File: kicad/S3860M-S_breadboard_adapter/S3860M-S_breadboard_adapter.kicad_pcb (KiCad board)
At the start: 2 copper layers, 26.9 x 36.3 mm, 4 parts, among them P1 CONN_01X12, P2 CONN_01X12, U1 XS3860

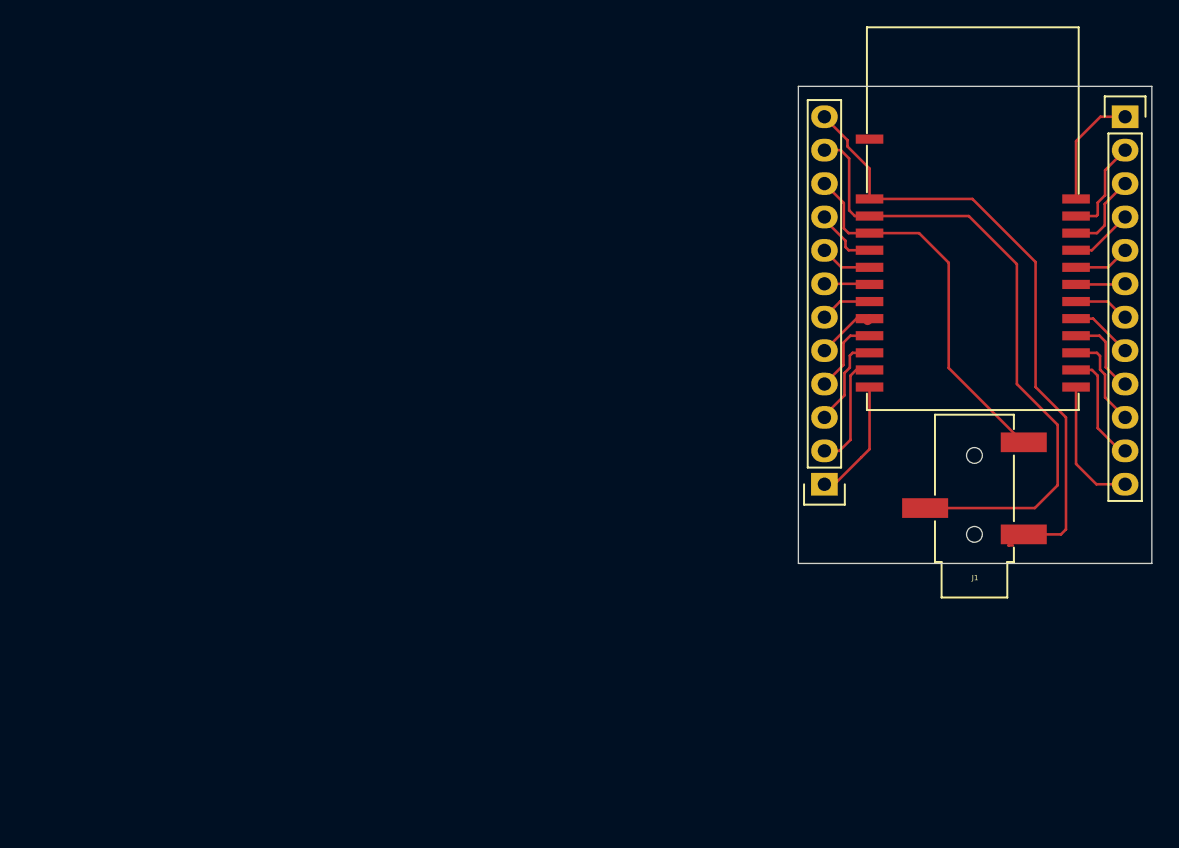
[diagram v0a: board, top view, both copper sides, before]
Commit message: 0805 resistors as jumpers for selecting module
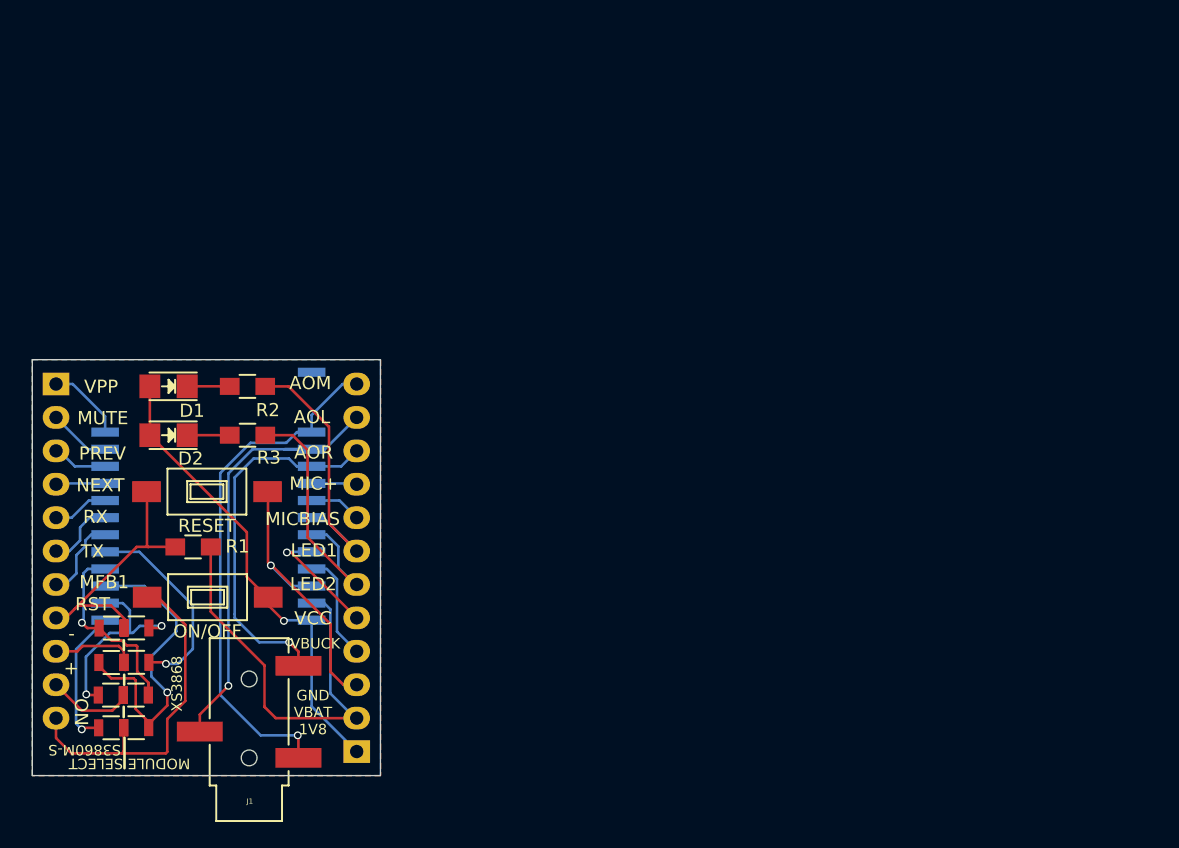
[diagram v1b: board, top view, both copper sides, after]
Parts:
- added D1: LED, LEDs:LED-1206, F.Cu at (94.9, 91.6)
- added D2: LED, LEDs:LED-1206, F.Cu at (94.9, 95.3)
- added ON/OFF: ON/OFF, Buttons_Switches_SMD:SW_SPST_FSMSM, F.Cu at (97.9, 107.6)
- added R1: 10k, Resistors_SMD:R_0805_HandSoldering, F.Cu at (96.8, 103.8)
- added R2: 470, Resistors_SMD:R_0805_HandSoldering, F.Cu at (100.9, 91.6)
- added R3: 470, Resistors_SMD:R_0805_HandSoldering, F.Cu at (100.9, 95.3)
- added RESET: 1, Buttons_Switches_SMD:SW_SPST_FSMSM, F.Cu at (97.8, 99.6)
- added SM_ONKEY1: 0, Resistors_SMD:R_0805, F.Cu at (90.6, 117.6)
- added SM_RESET1: 0, Resistors_SMD:R_0805, F.Cu at (90.6, 110.0)
- added SM_VOL+1: 0, Resistors_SMD:R_0805, F.Cu at (90.5, 115.1)
- added SM_VOL-1: 0, Resistors_SMD:R_0805, F.Cu at (90.6, 112.6)
- added XS_ONKEY1: 0, Resistors_SMD:R_0805, F.Cu at (92.5, 117.6)
- added XS_RESET1: 0, Resistors_SMD:R_0805, F.Cu at (92.5, 110.0)
- added XS_VOL+1: 0, Resistors_SMD:R_0805, F.Cu at (92.4, 115.1)
- added XS_VOL-1: 0, Resistors_SMD:R_0805, F.Cu at (92.5, 112.6)
- J1: value (none) -> SCJ368R1NUS0B00G
- P1: moved to B.Cu
- P2: footprint Pin_Headers:Pin_Header_Straight_1x12 -> Pin_Headers:Pin_Header_Straight_1x11; moved to B.Cu
- U1: value XS3860 -> XS3868; moved to B.Cu
- moved P2 83.8 mm to (86.4, 91.4), turned to 180 degrees
- moved J1 57.7 mm to (101.0, 119.9)
- moved U1 46.0 mm to (105.8, 110.9), turned to 180 degrees
- moved P1 41.0 mm to (109.2, 119.4), turned to 0 degrees
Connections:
- P2 pad 10: Net-(P2-Pad10) -> /VOL+
- P2 pad 11: Net-(P2-Pad11) -> /ONKEY
- P2 pad 8: Net-(P2-Pad8) -> /RESET
- P2 pad 9: Net-(P2-Pad9) -> /VOL-
- U1 pad 14: Net-(P2-Pad12) -> Net-(SM_ONKEY1-Pad2)
- U1 pad 15: Net-(P2-Pad11) -> Net-(SM_VOL+1-Pad2)
- U1 pad 16: Net-(P2-Pad10) -> Net-(SM_VOL-1-Pad2)
- U1 pad 17: Net-(P2-Pad9) -> Net-(SM_RESET1-Pad2)
- U1 pad 18: Net-(P2-Pad8) -> Net-(U1-Pad18)
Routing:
- net /ONKEY: track 0.00 -> 27.3 mm
- net Net-(D1-Pad2): track 9.26 -> 35.8 mm, vias 0 -> 1
- net Net-(SM_VOL-1-Pad2): track 0.00 -> 24.5 mm, vias 0 -> 1
- net Net-(P1-Pad2): track 8.84 -> 32.0 mm
- net /RESET: track 0.00 -> 20.6 mm
- net Net-(P1-Pad6): track 3.92 -> 21.5 mm
- net Net-(P1-Pad7): track 3.45 -> 20.9 mm
- net Net-(U1-Pad18): track 0.00 -> 17.1 mm, vias 0 -> 1
- net Net-(SM_VOL+1-Pad2): track 0.00 -> 15.6 mm, vias 0 -> 2
- net Net-(P1-Pad3): track 7.09 -> 21.9 mm, vias 0 -> 1
- net Net-(SM_RESET1-Pad2): track 0.00 -> 14.8 mm, vias 0 -> 1
- net Net-(J1-Pad2): track 49.4 -> 36.2 mm, vias 0 -> 1
- net Net-(SM_ONKEY1-Pad2): track 0.00 -> 10.7 mm, vias 0 -> 1
- net Net-(P2-Pad12): track 10.2 -> 0.00 mm
- net Net-(P2-Pad11): track 8.62 -> 0.00 mm
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- added copper zone on B.Cu, net Net-(P1-Pad3)
- added copper zone on F.Cu, net Net-(P1-Pad3)
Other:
- board size 26.9 x 36.3 mm -> 26.5 x 31.6 mm
- board text added: "+"
- board text added: "-"
- board text added: "AOL"
- board text added: "AOM"
- board text added: "AOR"
- board text added: "GND VBAT 1V8"
- board text added: "LED1"
- board text added: "LED2"
- board text added: "MFB1"
- board text added: "MIC+"
- board text added: "MICBIAS"
- board text added: "MODULE SELECT"
- board text added: "MUTE"
- board text added: "NEXT"
- board text added: "ON"
- board text added: "PREV"
- board text added: "RST"
- board text added: "RX"
- board text added: "S3860M-S"
- board text added: "TX"
- board text added: "VBUCK"
- board text added: "VCC"
- board text added: "VPP"
- board text added: "XS3868"

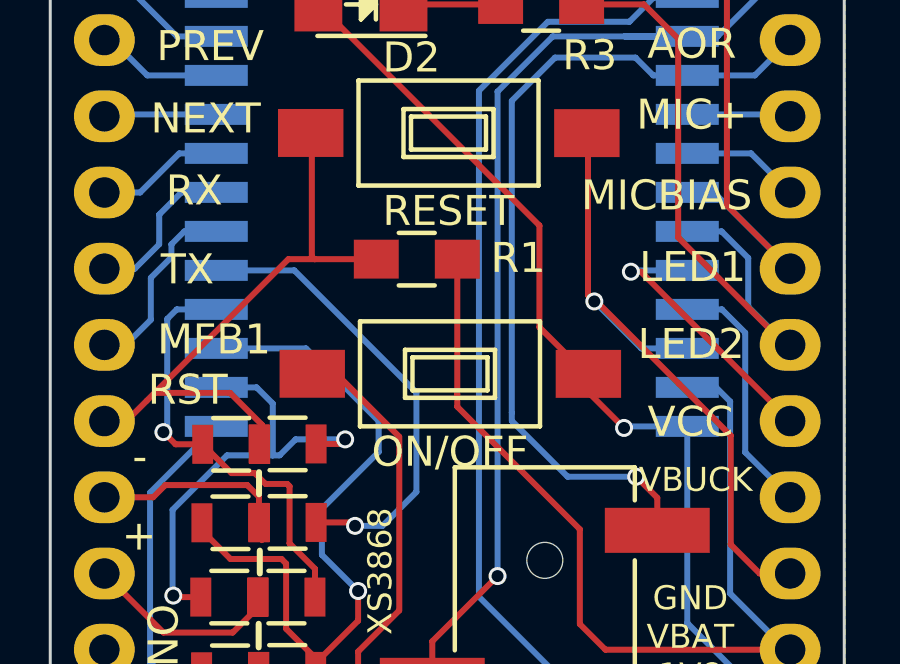
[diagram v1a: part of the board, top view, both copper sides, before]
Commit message: change jumper resistors to select module from 0402 to 0805, corect name for jack is PJ320B
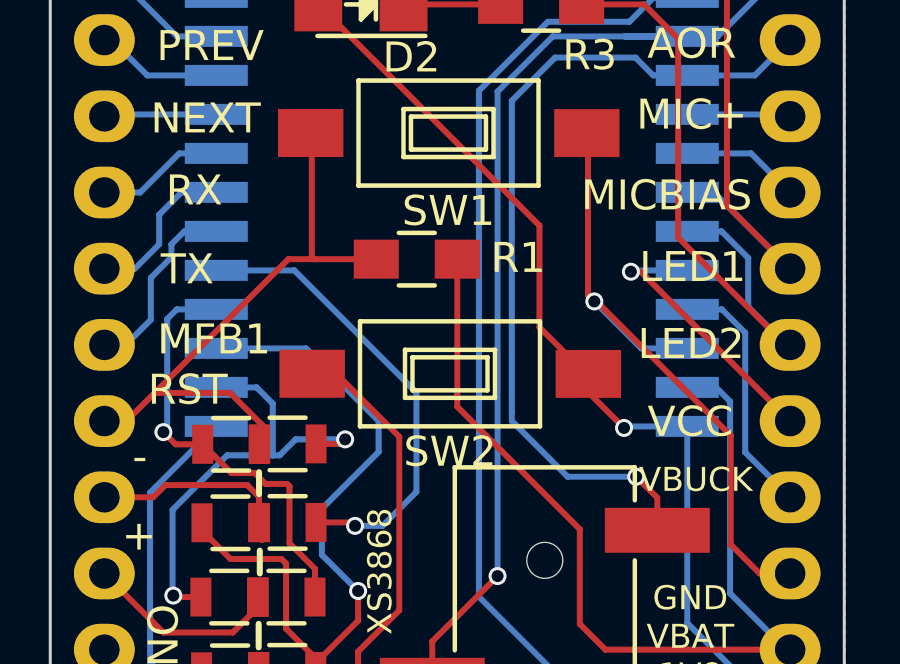
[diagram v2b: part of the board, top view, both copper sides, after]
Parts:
- J1: footprint jacks:3.5mm_stereo_jack_PJ3020B -> jacks:3.5mm_stereo_jack_PJ320B
- renumbered RESET to SW1, ON/OFF to SW2
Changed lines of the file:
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@@
     (visible_elements FFFEFF3F)
     (pcbplotparams
-      (layerselection 0x00000_00000001)
+      (layerselection 0x00030_ffffffff)
       (usegerberextensions false)
       (excludeedgelayer true)
@@
       (padsonsilk false)
       (subtractmaskfromsilk false)
-      (outputformat 4)
+      (outputformat 5)
       (mirror false)
       (drillshape 2)
@@
       (net 26 "Net-(SM_ONKEY1-Pad2)"))
   )
-  (module jacks:3.5mm_stereo_jack_PJ3020B (layer F.Cu)
-    (at 101.0412 119.8626 180)
-    (fp_text reference J1 (at -0.05 -3.3 180) (layer F.SilkS)
-      (effects (font (size 0.39878 0.39878) (thickness 0.0508)))
-    )
-    (fp_text value SCJ368R1NUS0B00G (at 0.11 2.15 270) (layer F.SilkS) hide
-      (effects (font (thickness 0.3048)))
-    )
-    (fp_line (start 3 3) (end 3 9.1) (layer F.SilkS) (width 0.15))
-    (fp_line (start 3 9.1) (end -3 9.1) (layer F.SilkS) (width 0.15))
-    (fp_line (start -3 9.1) (end -3 8) (layer F.SilkS) (width 0.15))
-    (fp_line (start -3 1) (end -3 6) (layer F.SilkS) (width 0.15))
-    (fp_line (start -3 -1) (end -3 -2.1) (layer F.SilkS) (width 0.15))
-    (fp_line (start -3 -2.1) (end -2.5 -2.1) (layer F.SilkS) (width 0.15))
-    (fp_line (start -2.5 -2.1) (end -2.5 -4.8) (layer F.SilkS) (width 0.15))
-    (fp_line (start -2.5 -4.8) (end 2.5 -4.8) (layer F.SilkS) (width 0.15))
-    (fp_line (start 2.5 -4.8) (end 2.5 -2.1) (layer F.SilkS) (width 0.15))
-    (fp_line (start 2.5 -2.1) (end 3 -2.1) (layer F.SilkS) (width 0.15))
-    (fp_line (start 3 -2.1) (end 3 1) (layer F.SilkS) (width 0.15))
-    (pad "" np_thru_hole circle (at 0 6 180) (size 1.2 1.2) (drill 1.2) (layers *.Cu *.Mask F.SilkS))
-    (pad 5 smd rect (at -3.75 7 180) (size 3.5 1.5) (layers F.Cu F.Paste F.Mask)
-      (net 3 "Net-(J1-Pad5)"))
-    (pad 2 smd rect (at 3.75 2 180) (size 3.5 1.5) (layers F.Cu F.Paste F.Mask)
-      (net 2 "Net-(J1-Pad2)"))
-    (pad 1 smd rect (at -3.75 0 180) (size 3.5 1.5) (layers F.Cu F.Paste F.Mask)
-      (net 1 "Net-(J1-Pad1)"))
-    (pad "" np_thru_hole circle (at 0 0 180) (size 1.2 1.2) (drill 1.2) (layers *.Cu *.Mask F.SilkS))
-  )
   (module LEDs:LED-1206 (layer F.Cu)
     (at 94.91218 91.61526 180)
@@
     (tags "SPST button tactile switch")
     (attr smd)
-    (fp_text reference RESET (at 0.01011 -2.60022 180) (layer F.SilkS)
+    (fp_text reference SW1 (at 0.01011 -2.60022 180) (layer F.SilkS)
       (effects (font (size 1 1) (thickness 0.15)))
     )
@@
     (tags "SPST button tactile switch")
     (attr smd)
-    (fp_text reference ON/OFF (at 0.01011 -2.60022 180) (layer F.SilkS)
+    (fp_text reference SW2 (at 0.01011 -2.60022 180) (layer F.SilkS)
       (effects (font (size 1 1) (thickness 0.15)))
     )
@@
     )
   )
+  (module jacks:3.5mm_stereo_jack_PJ320B (layer F.Cu)
+    (at 101.0412 119.8626 180)
+    (fp_text reference J1 (at -0.05 -3.3 180) (layer F.SilkS)
+      (effects (font (size 0.39878 0.39878) (thickness 0.0508)))
+    )
+    (fp_text value SCJ368R1NUS0B00G (at 0.11 2.15 270) (layer F.SilkS) hide
+      (effects (font (thickness 0.3048)))
+    )
+    (fp_line (start 3 3) (end 3 9.1) (layer F.SilkS) (width 0.15))
+    (fp_line (start 3 9.1) (end -3 9.1) (layer F.SilkS) (width 0.15))
+    (fp_line (start -3 9.1) (end -3 8) (layer F.SilkS) (width 0.15))
+    (fp_line (start -3 1) (end -3 6) (layer F.SilkS) (width 0.15))
+    (fp_line (start -3 -1) (end -3 -2.1) (layer F.SilkS) (width 0.15))
+    (fp_line (start -3 -2.1) (end -2.5 -2.1) (layer F.SilkS) (width 0.15))
+    (fp_line (start -2.5 -2.1) (end -2.5 -4.8) (layer F.SilkS) (width 0.15))
+    (fp_line (start -2.5 -4.8) (end 2.5 -4.8) (layer F.SilkS) (width 0.15))
+    (fp_line (start 2.5 -4.8) (end 2.5 -2.1) (layer F.SilkS) (width 0.15))
+    (fp_line (start 2.5 -2.1) (end 3 -2.1) (layer F.SilkS) (width 0.15))
+    (fp_line (start 3 -2.1) (end 3 1) (layer F.SilkS) (width 0.15))
+    (pad "" np_thru_hole circle (at 0 6 180) (size 1.2 1.2) (drill 1.2) (layers *.Cu *.Mask F.SilkS))
+    (pad 5 smd rect (at -3.75 7 180) (size 3.5 1.5) (layers F.Cu F.Paste F.Mask)
+      (net 3 "Net-(J1-Pad5)"))
+    (pad 2 smd rect (at 3.75 2 180) (size 3.5 1.5) (layers F.Cu F.Paste F.Mask)
+      (net 2 "Net-(J1-Pad2)"))
+    (pad 1 smd rect (at -3.75 0 180) (size 3.5 1.5) (layers F.Cu F.Paste F.Mask)
+      (net 1 "Net-(J1-Pad1)"))
+    (pad "" np_thru_hole circle (at 0 0 180) (size 1.2 1.2) (drill 1.2) (layers *.Cu *.Mask F.SilkS))
+  )
   (gr_text ON (at 88.265 116.3701 270) (layer F.SilkS)

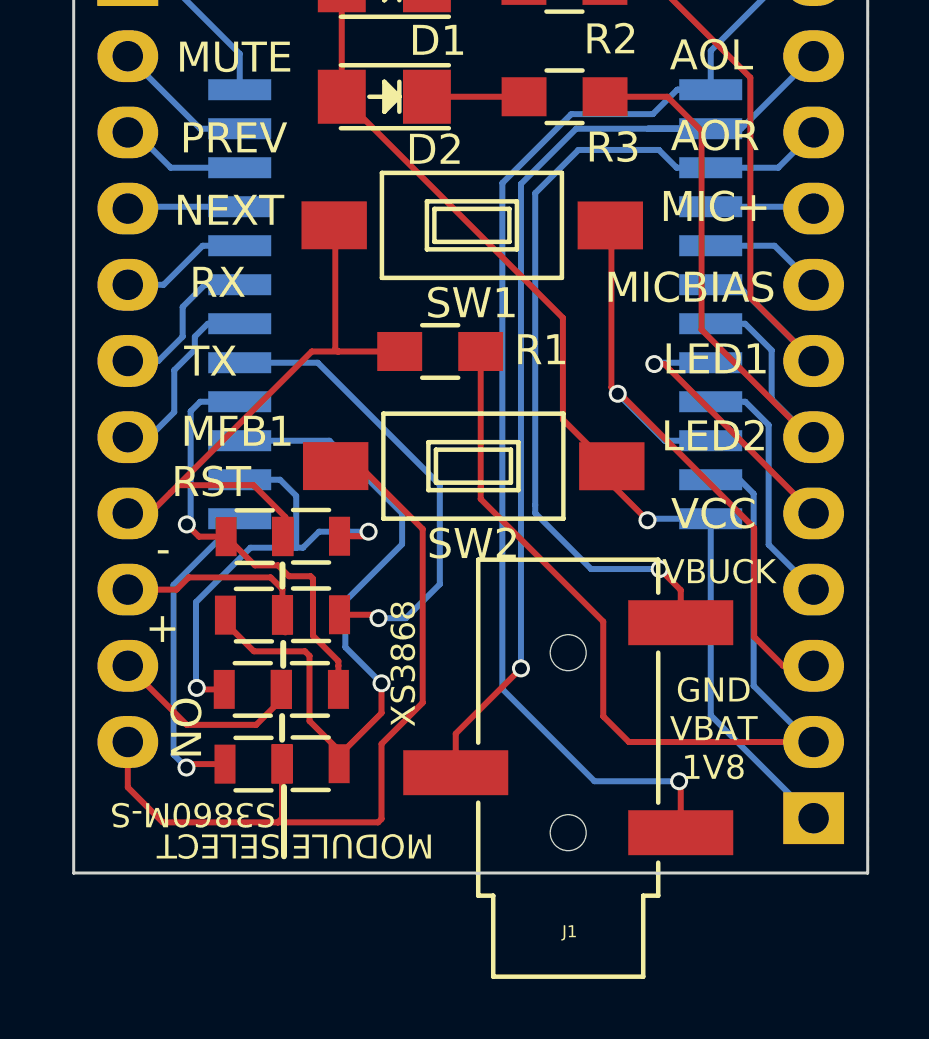
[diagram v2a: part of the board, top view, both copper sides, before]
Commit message: update for GND/VBUCK diffrence betwen S3860M-S and XS3868 module, using sMD jumpers  for selection betwen modules
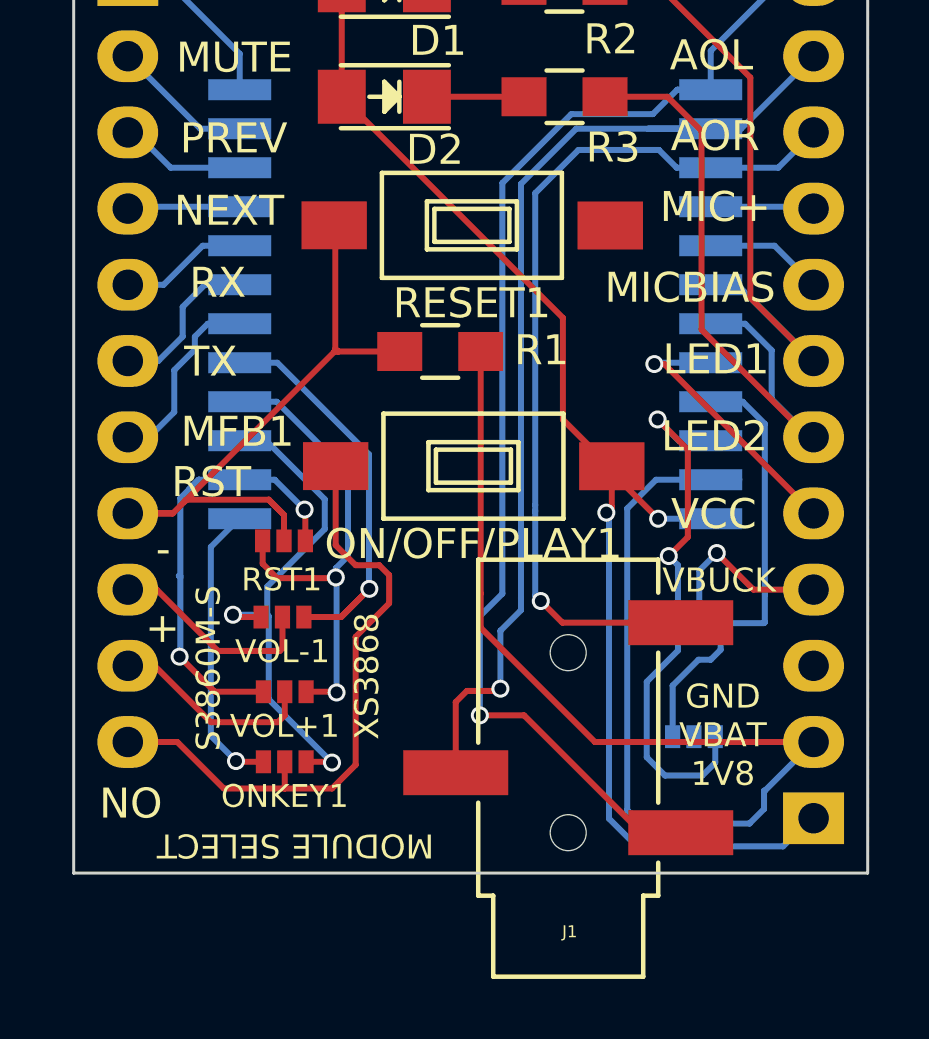
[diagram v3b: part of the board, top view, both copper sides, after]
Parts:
- removed SM_ONKEY1, SM_RESET1, SM_VOL+1, SM_VOL-1, XS_ONKEY1, XS_RESET1, XS_VOL+1, XS_VOL-1: 0, Resistors_SMD:R_0805
- added GND1: GND, open-project:S_JUMPER_3, B.Cu at (105.2, 116.7)
- added ONKEY1: ONKEY, open-project:S_JUMPER_3, F.Cu at (91.6, 117.5)
- added RST1: RST, open-project:S_JUMPER_3, F.Cu at (91.6, 110.1)
- added VBUCK1: VBUCK, open-project:S_JUMPER_3, B.Cu at (105.4, 112.9)
- added VOL+1: VOL+, open-project:S_JUMPER_3, F.Cu at (91.6, 115.2)
- added VOL-1: VOL-, open-project:S_JUMPER_3, F.Cu at (91.5, 112.7)
- U1: value XS3868 -> S3860M-S
- renumbered SW2 to ON/OFF/PLAY1, SW1 to RESET1
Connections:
- P1 pad 3: Net-(P1-Pad3) -> /GND
- P1 pad 4: Net-(P1-Pad4) -> /VBUCK
- RESET1 pad 1: Net-(P1-Pad3) -> /GND
- U1 pad 10: Net-(P1-Pad4) -> Net-(GND1-Pad3)
- U1 pad 11: Net-(P1-Pad3) -> Net-(GND1-Pad1)
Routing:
- net Net-(P1-Pad3): track 21.9 -> 0.00 mm, vias 1 -> 0
- net Net-(GND1-Pad1): track 0.00 -> 18.1 mm, vias 0 -> 2
- net Net-(GND1-Pad3): track 0.00 -> 14.9 mm
- net Net-(P1-Pad2): track 32.0 -> 44.0 mm
- net Net-(D1-Pad2): track 35.8 -> 44.9 mm, vias 1 -> 2
- net Net-(P1-Pad4): track 8.36 -> 0.00 mm
- net Net-(ONKEY1-Pad1): track 24.5 -> 17.1 mm, vias 1 -> 2
- net /VBUCK: track 0.00 -> 7.06 mm, vias 0 -> 1
- net /ONKEY: track 27.3 -> 23.6 mm
- net Net-(J1-Pad5): track 28.3 -> 30.4 mm
- net Net-(J1-Pad1): track 41.0 -> 42.8 mm
- net Net-(RST1-Pad3): track 14.8 -> 16.5 mm, vias 1 -> 2
- net /RESET: track 20.6 -> 22.2 mm
- net Net-(U1-Pad18): track 17.1 -> 15.5 mm
- net Net-(ONKEY1-Pad3): track 10.7 -> 9.76 mm
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- added copper zone on B.Cu, net /GND
- added copper zone on F.Cu, net /GND
- removed copper zone on B.Cu, net Net-(P1-Pad3)
- removed copper zone on F.Cu, net Net-(P1-Pad3)
